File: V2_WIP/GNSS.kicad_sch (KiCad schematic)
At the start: 16 parts, among them J301 USB_B_Micro, U301 USBLC6-2SC6, U401 NEO-M9N

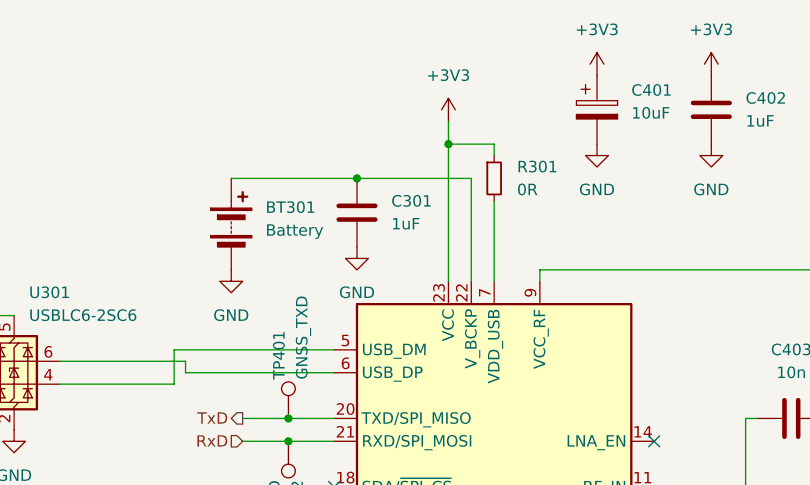
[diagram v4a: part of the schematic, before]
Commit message: fixed errors in schematic
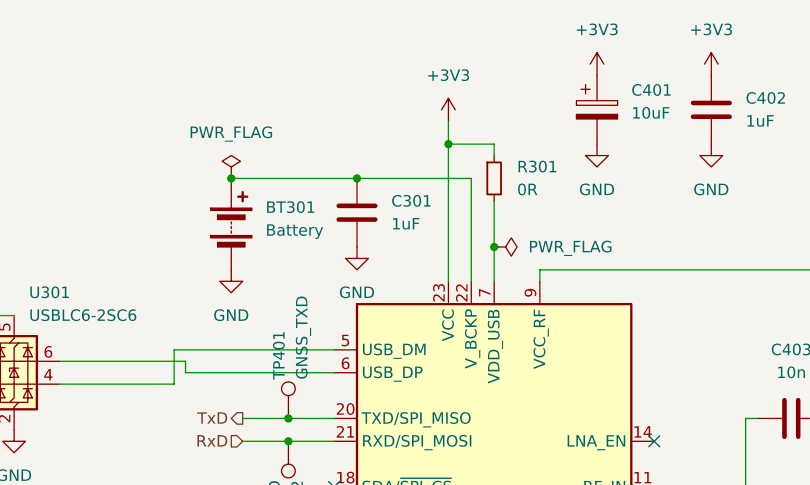
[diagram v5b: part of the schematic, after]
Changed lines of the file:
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@@
+	)
+	(junction
+		(at 139.7 81.28)
+		(diameter 0)
+		(color 0 0 0 0)
 	)
 	(junction
@@
 	)
 	(junction
+		(at 110.49 73.66)
+		(diameter 0)
+		(color 0 0 0 0)
+	)
+	(junction
 		(at 116.84 100.33)
 		(diameter 0)
@@
 	(wire
 		(pts
+			(xy 139.7 81.28) (xy 139.7 76.2)
+		)
+		(stroke
+			(width 0)
+			(type default)
+		)
+	)
+	(wire
+		(pts
 			(xy 137.16 73.66) (xy 137.16 85.09)
 		)
@@
 	(wire
 		(pts
-			(xy 139.7 85.09) (xy 139.7 76.2)
+			(xy 139.7 85.09) (xy 139.7 81.28)
 		)
 		(stroke
@@
 	)
 	(symbol
+		(lib_id "power:PWR_FLAG")
+		(at 139.7 81.28 270)
+		(unit 1)
+		(exclude_from_sim no)
+		(in_bom yes)
+		(on_board yes)
+		(dnp no)
+		(fields_autoplaced yes)
+		(property "Reference" "#FLG0302"
+			(at 141.605 81.28 0)
+			(effects
+				(font
+					(size 1.27 1.27)
+				)
+				(hide yes)
+			)
+		)
+		(property "Value" "PWR_FLAG"
+			(at 143.51 81.2799 90)
+			(effects
+				(font
+					(size 1.27 1.27)
+				)
+				(justify left)
+			)
+		)
+		(property "Footprint" ""
+			(at 139.7 81.28 0)
+			(effects
+				(font
+					(size 1.27 1.27)
+				)
+				(hide yes)
+			)
+		)
+		(property "Datasheet" "~"
+			(at 139.7 81.28 0)
+			(effects
+				(font
+					(size 1.27 1.27)
+				)
+				(hide yes)
+			)
+		)
+		(property "Description" "Special symbol for telling ERC where power comes from"
+			(at 139.7 81.28 0)
+			(effects
+				(font
+					(size 1.27 1.27)
+				)
+				(hide yes)
+			)
+		)
+		(pin "1"
+		)
+		(instances
+			(project "gps"
+				(path "/00526ddc-5304-4072-af1e-192a9e7e83da/5cdf5b9a-bc05-4fbb-ac1a-8c1a969964f2"
+					(reference "#FLG0302")
+					(unit 1)
+				)
+			)
+		)
+	)
+	(symbol
 		(lib_id "Device:C_Polarized")
 		(at 151.13 66.04 0)
@@
 					(unit 1)
 				)
+			)
+		)
+	)
+	(symbol
+		(lib_id "power:PWR_FLAG")
+		(at 110.49 73.66 0)
+		(unit 1)
+		(exclude_from_sim no)
+		(in_bom yes)
+		(on_board yes)
+		(dnp no)
+		(fields_autoplaced yes)
+		(property "Reference" "#FLG0301"
+			(at 110.49 71.755 0)
+			(effects
+				(font
+					(size 1.27 1.27)
+				)
+				(hide yes)
+			)
+		)
+		(property "Value" "PWR_FLAG"
+			(at 110.49 68.58 0)
+			(effects
+				(font
+					(size 1.27 1.27)
+				)
+			)
+		)
+		(property "Footprint" ""
+			(at 110.49 73.66 0)
+			(effects
+				(font
+					(size 1.27 1.27)
+				)
+				(hide yes)
+			)
+		)
+		(property "Datasheet" "~"
+			(at 110.49 73.66 0)
+			(effects
+				(font
+					(size 1.27 1.27)
+				)
+				(hide yes)
+			)
+		)
+		(property "Description" "Special symbol for telling ERC where power comes from"
+			(at 110.49 73.66 0)
+			(effects
+				(font
+					(size 1.27 1.27)
+				)
+				(hide yes)
+			)
+		)
+		(pin "1"
+		)
+		(instances
+			(project ""
+				(path "/00526ddc-5304-4072-af1e-192a9e7e83da/5cdf5b9a-bc05-4fbb-ac1a-8c1a969964f2"
+					(reference "#FLG0301")
+					(unit 1)
+				)

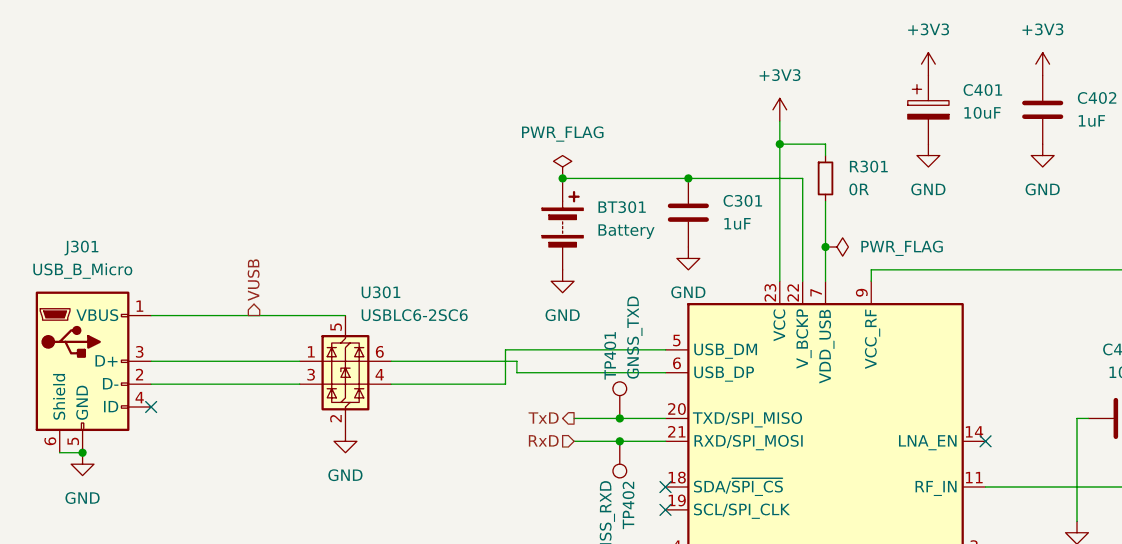
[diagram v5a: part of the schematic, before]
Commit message: Removed EEPROM, Adjusted Flash connection, renamed ESP pins and several other signals
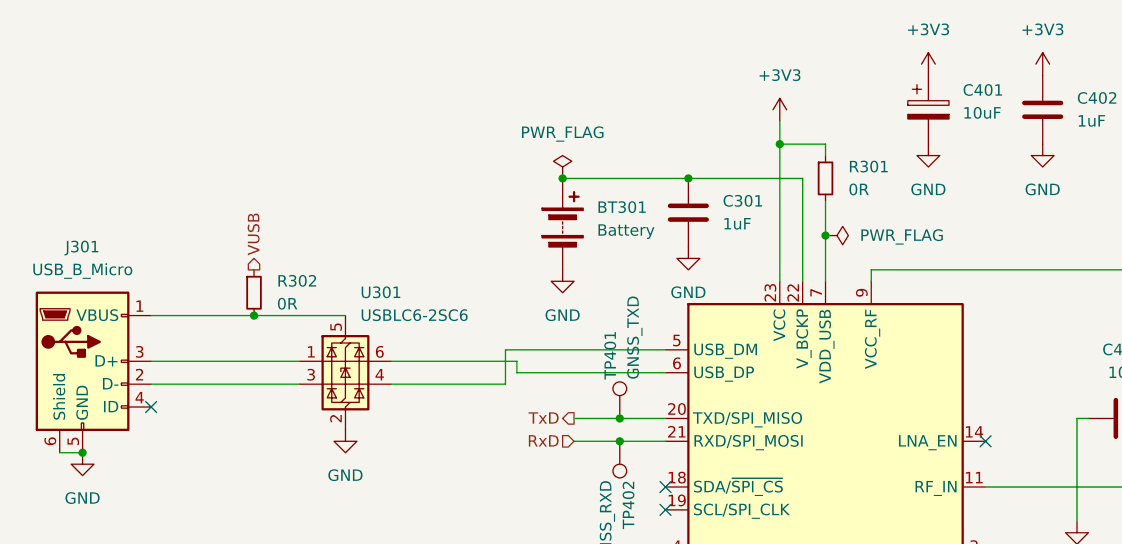
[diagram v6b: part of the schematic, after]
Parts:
- added R302: 0R, Resistor_SMD:R_0603_1608Metric_Pad0.98x0.95mm_HandSolder, symbol Device:R_Small
- J301: footprint KiCad:USB3145301A -> Connector_USB:USB_Micro-B_Wuerth_629105150521_CircularHoles
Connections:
- net VUSB: now also R302.1; no longer J301.1 (VBUS), U301.5 (VBUS)
- new net: J301.1 (VBUS), R302.2, U301.5 (VBUS)
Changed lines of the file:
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@@
+	)
+	(junction
+		(at 76.2 88.9)
+		(diameter 0)
+		(color 0 0 0 0)
 	)
 	(junction
@@
 	)
 	(junction
-		(at 139.7 81.28)
-		(diameter 0)
-		(color 0 0 0 0)
-	)
-	(junction
 		(at 134.62 69.85)
 		(diameter 0)
@@
 		(color 0 0 0 0)
 	)
+	(junction
+		(at 139.7 80.01)
+		(diameter 0)
+		(color 0 0 0 0)
+	)
 	(no_connect
 		(at 121.92 115.57)
@@
 	(wire
 		(pts
-			(xy 64.77 88.9) (xy 86.36 88.9)
+			(xy 64.77 88.9) (xy 76.2 88.9)
 		)
 		(stroke
@@
 	(wire
 		(pts
-			(xy 139.7 81.28) (xy 139.7 76.2)
-		)
-		(stroke
-			(width 0)
-			(type default)
-		)
-	)
-	(wire
-		(pts
 			(xy 137.16 73.66) (xy 137.16 85.09)
 		)
@@
 	(wire
 		(pts
-			(xy 139.7 85.09) (xy 139.7 81.28)
-		)
-		(stroke
-			(width 0)
-			(type default)
-		)
-	)
-	(wire
-		(pts
 			(xy 111.76 102.87) (xy 116.84 102.87)
 		)
@@
 	(wire
 		(pts
+			(xy 139.7 80.01) (xy 139.7 85.09)
+		)
+		(stroke
+			(width 0)
+			(type default)
+		)
+	)
+	(wire
+		(pts
 			(xy 116.84 100.33) (xy 121.92 100.33)
 		)
@@
 	(wire
 		(pts
+			(xy 76.2 88.9) (xy 86.36 88.9)
+		)
+		(stroke
+			(width 0)
+			(type default)
+		)
+	)
+	(wire
+		(pts
 			(xy 179.07 83.82) (xy 179.07 88.9)
 		)
@@
 		(pts
 			(xy 144.78 83.82) (xy 144.78 85.09)
+		)
+		(stroke
+			(width 0)
+			(type default)
+		)
+	)
+	(wire
+		(pts
+			(xy 139.7 80.01) (xy 139.7 76.2)
 		)
 		(stroke
@@
 		)
 	)
+	(hierarchical_label "VUSB"
+		(shape output)
+		(at 76.2 83.82 90)
+		(fields_autoplaced yes)
+		(effects
+			(font
+				(size 1.27 1.27)
+			)
+			(justify left)
+		)
+	)
 	(hierarchical_label "Pulse"
 		(shape output)
@@
 		)
 	)
-	(hierarchical_label "VUSB"
-		(shape output)
-		(at 76.2 88.9 90)
-		(fields_autoplaced yes)
-		(effects
-			(font
-				(size 1.27 1.27)
-			)
-			(justify left)
-		)
-	)
 	(symbol
 		(lib_id "Device:L")
@@
 	(symbol
 		(lib_id "power:PWR_FLAG")
-		(at 139.7 81.28 270)
+		(at 139.7 80.01 270)
 		(unit 1)
 		(exclude_from_sim no)
@@
 		(fields_autoplaced yes)
 		(property "Reference" "#FLG0302"
-			(at 141.605 81.28 0)
+			(at 141.605 80.01 0)
 			(effects
 				(font
@@
 		)
 		(property "Value" "PWR_FLAG"
-			(at 143.51 81.2799 90)
+			(at 143.51 80.0099 90)
 			(effects
 				(font
@@
 		)
 		(property "Footprint" ""
-			(at 139.7 81.28 0)
+			(at 139.7 80.01 0)
 			(effects
 				(font
@@
 		)
 		(property "Datasheet" "~"
-			(at 139.7 81.28 0)
+			(at 139.7 80.01 0)
 			(effects
 				(font
@@
 		)
 		(property "Description" "Special symbol for telling ERC where power comes from"
-			(at 139.7 81.28 0)
+			(at 139.7 80.01 0)
 			(effects
 				(font
@@
 			)
 		)
-		(property "Footprint" "KiCad:USB3145301A"
+		(property "Footprint" "Connector_USB:USB_Micro-B_Wuerth_629105150521_CircularHoles"
 			(at 60.96 95.25 0)
 			(effects
@@
 					(unit 1)
 				)
+			)
+		)
+	)
+	(symbol
+		(lib_id "Device:R_Small")
+		(at 76.2 86.36 0)
+		(unit 1)
+		(exclude_from_sim no)
+		(in_bom yes)
+		(on_board yes)
+		(dnp no)
+		(fields_autoplaced yes)
+		(property "Reference" "R302"
+			(at 78.74 85.0899 0)
+			(effects
+				(font
+					(size 1.27 1.27)
+				)
+				(justify left)
+			)
+		)
+		(property "Value" "0R"
+			(at 78.74 87.6299 0)
+			(effects
+				(font
+					(size 1.27 1.27)
+				)
+				(justify left)
+			)
+		)
+		(property "Footprint" "Resistor_SMD:R_0603_1608Metric_Pad0.98x0.95mm_HandSolder"
+			(at 76.2 86.36 0)
+			(effects
+				(font
+					(size 1.27 1.27)
+				)
+				(hide yes)
+			)
+		)
+		(property "Datasheet" "~"
+			(at 76.2 86.36 0)
+			(effects
+				(font
+					(size 1.27 1.27)
+				)
+				(hide yes)
+			)
+		)
+		(property "Description" "Resistor, small symbol"
+			(at 76.2 86.36 0)
+			(effects
+				(font
+					(size 1.27 1.27)
+				)
+				(hide yes)
+			)
+		)
+		(pin "2"
+		)
+		(pin "1"
+		)
+		(instances
+			(project "gps"
+				(path "/00526ddc-5304-4072-af1e-192a9e7e83da/5cdf5b9a-bc05-4fbb-ac1a-8c1a969964f2"
+					(reference "R302")
+					(unit 1)
+				)

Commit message: minor changes
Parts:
- R302: now not fitted
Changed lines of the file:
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@@
+	(wire
+		(pts
+			(xy 76.2 86.36) (xy 76.2 88.9)
+		)
+		(stroke
+			(width 0)
+			(type default)
+		)
+	)
 	(wire
 		(pts
@@
 		(pts
 			(xy 134.62 69.85) (xy 134.62 85.09)
+		)
+		(stroke
+			(width 0)
+			(type default)
+		)
+	)
+	(wire
+		(pts
+			(xy 76.2 78.74) (xy 76.2 81.28)
 		)
 		(stroke
@@
 	(hierarchical_label "VUSB"
 		(shape output)
-		(at 76.2 83.82 90)
+		(at 76.2 78.74 90)
 		(fields_autoplaced yes)
 		(effects
@@
 	(symbol
 		(lib_id "Device:R_Small")
-		(at 76.2 86.36 0)
-		(unit 1)
-		(exclude_from_sim no)
-		(in_bom yes)
-		(on_board yes)
-		(dnp no)
+		(at 76.2 83.82 0)
+		(unit 1)
+		(exclude_from_sim no)
+		(in_bom yes)
+		(on_board yes)
+		(dnp yes)
 		(fields_autoplaced yes)
 		(property "Reference" "R302"
+			(at 78.74 82.5499 0)
+			(effects
+				(font
+					(size 1.27 1.27)
+				)
+				(justify left)
+			)
+		)
+		(property "Value" "0R"
 			(at 78.74 85.0899 0)
 			(effects
@@
 			)
 		)
-		(property "Value" "0R"
-			(at 78.74 87.6299 0)
-			(effects
-				(font
-					(size 1.27 1.27)
-				)
-				(justify left)
-			)
-		)
 		(property "Footprint" "Resistor_SMD:R_0603_1608Metric_Pad0.98x0.95mm_HandSolder"
-			(at 76.2 86.36 0)
+			(at 76.2 83.82 0)
 			(effects
 				(font
@@
 		)
 		(property "Datasheet" "~"
-			(at 76.2 86.36 0)
+			(at 76.2 83.82 0)
 			(effects
 				(font
@@
 		)
 		(property "Description" "Resistor, small symbol"
-			(at 76.2 86.36 0)
-			(effects
-				(font
+			(at 76.2 83.82 0)
+			(effects
+				(font

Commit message: finallizes schematic; pcb progress
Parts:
- removed R302: 0R, Resistor_SMD:R_0603_1608Metric_Pad0.98x0.95mm_HandSolder, symbol Device:R_Small
- added D301: M2, Diode_SMD:D_SMA, symbol Device:D
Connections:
- net VUSB: now also D301.1 (K)
- net at J301.1 (VBUS), U301.5 (VBUS): now also D301.2 (A)
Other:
- moved on the sheet: TP401, TP402
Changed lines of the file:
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@@
 	(paper "A4")
-	(junction
-		(at 116.84 102.87)
-		(diameter 0)
-		(color 0 0 0 0)
-	)
 	(junction
 		(at 179.07 107.95)
@@
 	)
 	(junction
+		(at 119.38 100.33)
+		(diameter 0)
+		(color 0 0 0 0)
+	)
+	(junction
 		(at 57.15 104.14)
 		(diameter 0)
@@
 	)
 	(junction
-		(at 116.84 100.33)
-		(diameter 0)
-		(color 0 0 0 0)
-	)
-	(junction
 		(at 179.07 100.33)
 		(diameter 0)
@@
 		(color 0 0 0 0)
 	)
+	(junction
+		(at 119.38 102.87)
+		(diameter 0)
+		(color 0 0 0 0)
+	)
 	(no_connect
 		(at 121.92 115.57)
@@
 	(wire
 		(pts
-			(xy 111.76 100.33) (xy 116.84 100.33)
+			(xy 76.2 77.47) (xy 76.2 78.74)
+		)
+		(stroke
+			(width 0)
+			(type default)
+		)
+	)
+	(wire
+		(pts
+			(xy 111.76 100.33) (xy 119.38 100.33)
 		)
 		(stroke
@@
 	(wire
 		(pts
+			(xy 119.38 102.87) (xy 121.92 102.87)
+		)
+		(stroke
+			(width 0)
+			(type default)
+		)
+	)
+	(wire
+		(pts
 			(xy 64.77 88.9) (xy 76.2 88.9)
 		)
@@
 	(wire
 		(pts
+			(xy 119.38 100.33) (xy 121.92 100.33)
+		)
+		(stroke
+			(width 0)
+			(type default)
+		)
+	)
+	(wire
+		(pts
 			(xy 104.14 92.71) (xy 104.14 96.52)
 		)
@@
 	(wire
 		(pts
-			(xy 76.2 78.74) (xy 76.2 81.28)
+			(xy 119.38 106.68) (xy 119.38 102.87)
 		)
 		(stroke
@@
 	(wire
 		(pts
-			(xy 116.84 102.87) (xy 121.92 102.87)
-		)
-		(stroke
-			(width 0)
-			(type default)
-		)
-	)
-	(wire
-		(pts
 			(xy 54.61 104.14) (xy 57.15 104.14)
 		)
@@
 	(wire
 		(pts
-			(xy 111.76 102.87) (xy 116.84 102.87)
+			(xy 111.76 102.87) (xy 119.38 102.87)
 		)
 		(stroke
@@
 	(wire
 		(pts
-			(xy 116.84 100.33) (xy 121.92 100.33)
-		)
-		(stroke
-			(width 0)
-			(type default)
-		)
-	)
-	(wire
-		(pts
 			(xy 179.07 96.52) (xy 179.07 100.33)
+		)
+		(stroke
+			(width 0)
+			(type default)
+		)
+	)
+	(wire
+		(pts
+			(xy 119.38 97.79) (xy 119.38 100.33)
 		)
 		(stroke
@@
 	(hierarchical_label "VUSB"
 		(shape output)
-		(at 76.2 78.74 90)
+		(at 76.2 77.47 90)
 		(fields_autoplaced yes)
 		(effects
@@
 	(symbol
 		(lib_id "Connector:TestPoint")
-		(at 116.84 100.33 0)
+		(at 119.38 97.79 90)
 		(unit 1)
 		(exclude_from_sim no)
@@
 		(dnp no)
 		(property "Reference" "TP401"
-			(at 115.824 96.012 90)
+			(at 115.062 98.806 90)
 			(effects
 				(font
@@
 		)
 		(property "Value" "GNSS_TXD"
-			(at 118.364 96.012 90)
+			(at 115.062 96.266 90)
 			(effects
 				(font
@@
 		)
 		(property "Footprint" "TestPoint:TestPoint_Pad_D1.5mm"
-			(at 121.92 100.33 0)
+			(at 119.38 92.71 0)
 			(effects
 				(font
@@
 		)
 		(property "Datasheet" "~"
-			(at 121.92 100.33 0)
+			(at 119.38 92.71 0)
 			(effects
 				(font
@@
 		)
 		(property "Description" "test point"
-			(at 116.84 100.33 0)
+			(at 119.38 97.79 0)
 			(effects
 				(font
@@
 	)
 	(symbol
+		(lib_id "Device:D")
+		(at 76.2 82.55 270)
+		(unit 1)
+		(exclude_from_sim no)
+		(in_bom yes)
+		(on_board yes)
+		(dnp no)
+		(fields_autoplaced yes)
+		(property "Reference" "D301"
+			(at 78.74 81.2799 90)
+			(effects
+				(font
+					(size 1.27 1.27)
+				)
+				(justify left)
+			)
+		)
+		(property "Value" "M2"
+			(at 78.74 83.8199 90)
+			(effects
+				(font
+					(size 1.27 1.27)
+				)
+				(justify left)
+			)
+		)
+		(property "Footprint" "Diode_SMD:D_SMA"
+			(at 76.2 82.55 0)
+			(effects
+				(font
+					(size 1.27 1.27)
+				)
+				(hide yes)
+			)
+		)
+		(property "Datasheet" "https://cz.mouser.com/ProductDetail/Diotec-Semiconductor/M2?qs=sGAEpiMZZMtbRapU8LlZDx2r3HTumQnibe%2FZmv21Qi%252BB2t1FfYiJ1Q%3D%3D"
+			(at 76.2 82.55 0)
+			(effects
+				(font
+					(size 1.27 1.27)
+				)
+				(hide yes)
+			)
+		)
+		(property "Description" "Diode"
+			(at 76.2 82.55 0)
+			(effects
+				(font
+					(size 1.27 1.27)
+				)
+				(hide yes)
+			)
+		)
+		(property "Sim.Device" "D"
+			(at 76.2 82.55 0)
+			(effects
+				(font
+					(size 1.27 1.27)
+				)
+				(hide yes)
+			)
+		)
+		(property "Sim.Pins" "1=K 2=A"
+			(at 76.2 82.55 0)
+			(effects
+				(font
+					(size 1.27 1.27)
+				)
+				(hide yes)
+			)
+		)
+		(pin "1"
+		)
+		(pin "2"
+		)
+		(instances
+			(project "gps"
+				(path "/00526ddc-5304-4072-af1e-192a9e7e83da/5cdf5b9a-bc05-4fbb-ac1a-8c1a969964f2"
+					(reference "D301")
+					(unit 1)
+				)
+			)
+		)
+	)
+	(symbol
 		(lib_id "Connector:USB_B_Micro")
 		(at 57.15 93.98 0)
@@
 	(symbol
 		(lib_id "Connector:TestPoint")
-		(at 116.84 102.87 180)
+		(at 119.38 106.68 90)
 		(unit 1)
 		(exclude_from_sim no)
@@
 		(dnp no)
 		(property "Reference" "TP402"
-			(at 117.856 107.188 90)
+			(at 115.062 107.696 90)
 			(effects
 				(font
@@
 		)
 		(property "Value" "GNSS_RXD"
-			(at 115.316 107.188 90)
+			(at 115.062 105.156 90)
 			(effects
 				(font
@@
 		)
 		(property "Footprint" "TestPoint:TestPoint_Pad_D1.5mm"
-			(at 111.76 102.87 0)
+			(at 119.38 101.6 0)
 			(effects
 				(font
@@
 		)
 		(property "Datasheet" "~"
-			(at 111.76 102.87 0)
+			(at 119.38 101.6 0)
 			(effects
 				(font
@@
 		)
 		(property "Description" "test point"
-			(at 116.84 102.87 0)
+			(at 119.38 106.68 0)
 			(effects
 				(font
@@
 					(unit 1)
 				)
-			)
-		)
-	)
-	(symbol
-		(lib_id "Device:R_Small")
-		(at 76.2 83.82 0)
-		(unit 1)
-		(exclude_from_sim no)
-		(in_bom yes)
-		(on_board yes)
-		(dnp yes)
-		(fields_autoplaced yes)
-		(property "Reference" "R302"
-			(at 78.74 82.5499 0)
-			(effects
-				(font
-					(size 1.27 1.27)
-				)
-				(justify left)
-			)
-		)
-		(property "Value" "0R"
-			(at 78.74 85.0899 0)
-			(effects
-				(font
-					(size 1.27 1.27)
-				)
-				(justify left)
-			)
-		)
-		(property "Footprint" "Resistor_SMD:R_0603_1608Metric_Pad0.98x0.95mm_HandSolder"
-			(at 76.2 83.82 0)
-			(effects
-				(font
-					(size 1.27 1.27)
-				)
-				(hide yes)
-			)
-		)
-		(property "Datasheet" "~"
-			(at 76.2 83.82 0)
-			(effects
-				(font
-					(size 1.27 1.27)
-				)
-				(hide yes)
-			)
-		)
-		(property "Description" "Resistor, small symbol"
-			(at 76.2 83.82 0)
-			(effects
-				(font
-					(size 1.27 1.27)
-				)
-				(hide yes)
-			)
-		)
-		(pin "2"
-		)
-		(pin "1"
-		)
-		(instances
-			(project "gps"
-				(path "/00526ddc-5304-4072-af1e-192a9e7e83da/5cdf5b9a-bc05-4fbb-ac1a-8c1a969964f2"
-					(reference "R302")
-					(unit 1)
-				)
